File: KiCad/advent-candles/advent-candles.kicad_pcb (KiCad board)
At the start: 2 copper layers, 10 parts, among them U1 ARDUINO_MINI

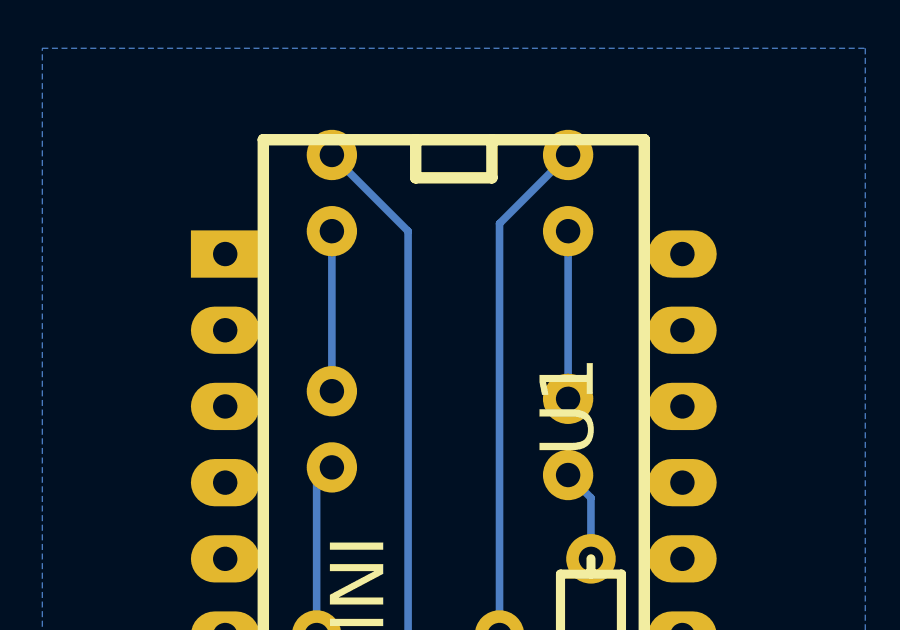
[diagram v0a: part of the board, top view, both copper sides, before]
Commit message: advent-candles: removed useless GND wires
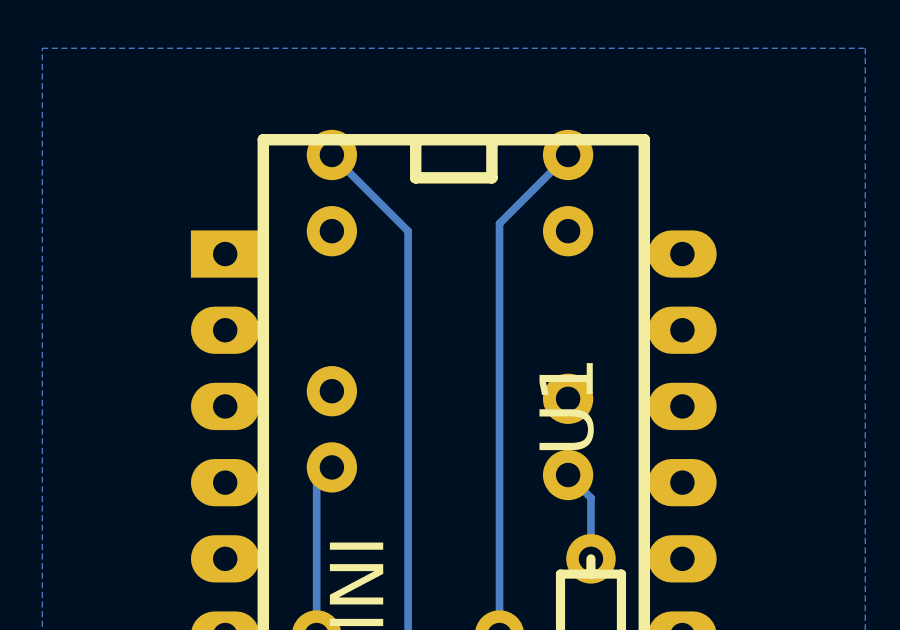
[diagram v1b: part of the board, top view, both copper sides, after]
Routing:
- net GND: track 10.9 -> 0.00 mm
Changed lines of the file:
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@@
     (thickness 1.6)
     (drawings 0)
-    (tracks 46)
+    (tracks 44)
     (zones 0)
     (modules 10)
@@
     )
   )
-  (segment (start 106.426 54.356) (end 106.426 48.768) (width 0.254) (layer B.Cu) (net 1))
-  (segment (start 98.552 54.102) (end 98.552 48.768) (width 0.254) (layer B.Cu) (net 1))
   (segment (start 104.14 62.23) (end 104.14 48.514) (width 0.254) (layer B.Cu) (net 2))
   (segment (start 104.14 48.514) (end 106.426 46.228) (width 0.254) (layer B.Cu) (net 2))
@@
   (segment (start 101.092 64.77) (end 101.092 48.768) (width 0.254) (layer B.Cu) (net 6))
   (segment (start 101.092 48.768) (end 98.552 46.228) (width 0.254) (layer B.Cu) (net 6))
-  (segment (start 94.996 69.85) (end 93.726 69.85) (width 0.254) (layer B.Cu) (net 7) (status 400000))
+  (segment (start 94.996 69.85) (end 93.726 69.85) (width 0.254) (layer B.Cu) (net 7))
   (segment (start 92.456 77.47) (end 93.345 76.581) (width 0.254) (layer B.Cu) (net 7))
   (segment (start 93.345 76.581) (end 93.345 70.231) (width 0.254) (layer B.Cu) (net 7))
   (segment (start 93.345 70.231) (end 93.726 69.85) (width 0.254) (layer B.Cu) (net 7))
-  (segment (start 92.456 77.47) (end 91.186 77.47) (width 0.254) (layer B.Cu) (net 7) (status 800000))
-  (segment (start 93.98 69.85) (end 94.996 69.85) (width 0.254) (layer B.Cu) (net 7) (status C00000))
-  (segment (start 91.186 80.01) (end 92.202 80.01) (width 0.254) (layer B.Cu) (net 8) (status 400000))
-  (segment (start 104.14 74.93) (end 110.236 74.93) (width 0.254) (layer B.Cu) (net 8) (status 800000))
+  (segment (start 92.456 77.47) (end 91.186 77.47) (width 0.254) (layer B.Cu) (net 7))
+  (segment (start 93.98 69.85) (end 94.996 69.85) (width 0.254) (layer B.Cu) (net 7))
+  (segment (start 91.186 80.01) (end 92.202 80.01) (width 0.254) (layer B.Cu) (net 8))
+  (segment (start 104.14 74.93) (end 110.236 74.93) (width 0.254) (layer B.Cu) (net 8))
   (segment (start 100.33 78.74) (end 104.14 74.93) (width 0.254) (layer B.Cu) (net 8))
   (segment (start 93.472 78.74) (end 100.33 78.74) (width 0.254) (layer B.Cu) (net 8))
@@
   (segment (start 107.188 59.69) (end 107.188 57.658) (width 0.254) (layer B.Cu) (net 9))
   (segment (start 107.188 57.658) (end 106.426 56.896) (width 0.254) (layer B.Cu) (net 9))
-  (segment (start 91.186 72.39) (end 92.075 72.39) (width 0.254) (layer B.Cu) (net 10) (status 400000))
-  (segment (start 96.266 77.47) (end 94.996 77.47) (width 0.254) (layer B.Cu) (net 10) (status 800000))
+  (segment (start 91.186 72.39) (end 92.075 72.39) (width 0.254) (layer B.Cu) (net 10))
+  (segment (start 96.266 77.47) (end 94.996 77.47) (width 0.254) (layer B.Cu) (net 10))
   (segment (start 96.647 77.089) (end 96.266 77.47) (width 0.254) (layer B.Cu) (net 10))
   (segment (start 96.647 66.802) (end 96.647 77.089) (width 0.254) (layer B.Cu) (net 10))
@@
   (segment (start 92.329 72.136) (end 92.329 67.818) (width 0.254) (layer B.Cu) (net 10))
   (segment (start 92.075 72.39) (end 92.329 72.136) (width 0.254) (layer B.Cu) (net 10))
-  (segment (start 91.186 74.93) (end 92.075 74.93) (width 0.254) (layer B.Cu) (net 11) (status 400000))
-  (segment (start 93.726 67.31) (end 94.996 67.31) (width 0.254) (layer B.Cu) (net 11) (status 800000))
+  (segment (start 91.186 74.93) (end 92.075 74.93) (width 0.254) (layer B.Cu) (net 11))
+  (segment (start 93.726 67.31) (end 94.996 67.31) (width 0.254) (layer B.Cu) (net 11))
   (segment (start 92.837 68.199) (end 93.726 67.31) (width 0.254) (layer B.Cu) (net 11))
   (segment (start 92.837 74.168) (end 92.837 68.199) (width 0.254) (layer B.Cu) (net 11))
